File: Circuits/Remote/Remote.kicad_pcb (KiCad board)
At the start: 2 copper layers, 84 x 64 mm, 33 parts, among them CN1 WRITER, Q1 2SK4017, SW1 WakeUp, U1 TWE_LITE_SMD, U2 STEPUPDIP3.3V, U3 ATP3011-PU, U4 HT82V739

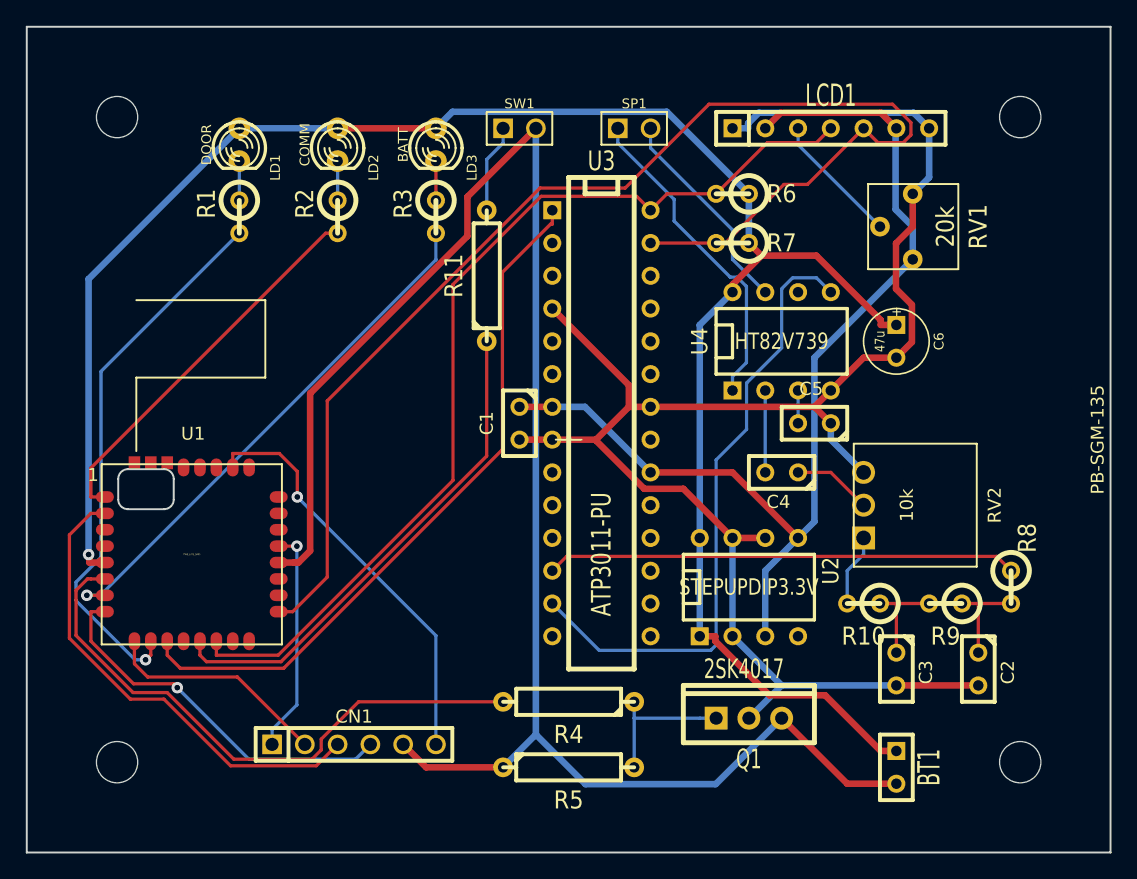
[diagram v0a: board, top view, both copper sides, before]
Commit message: Moved ATP.
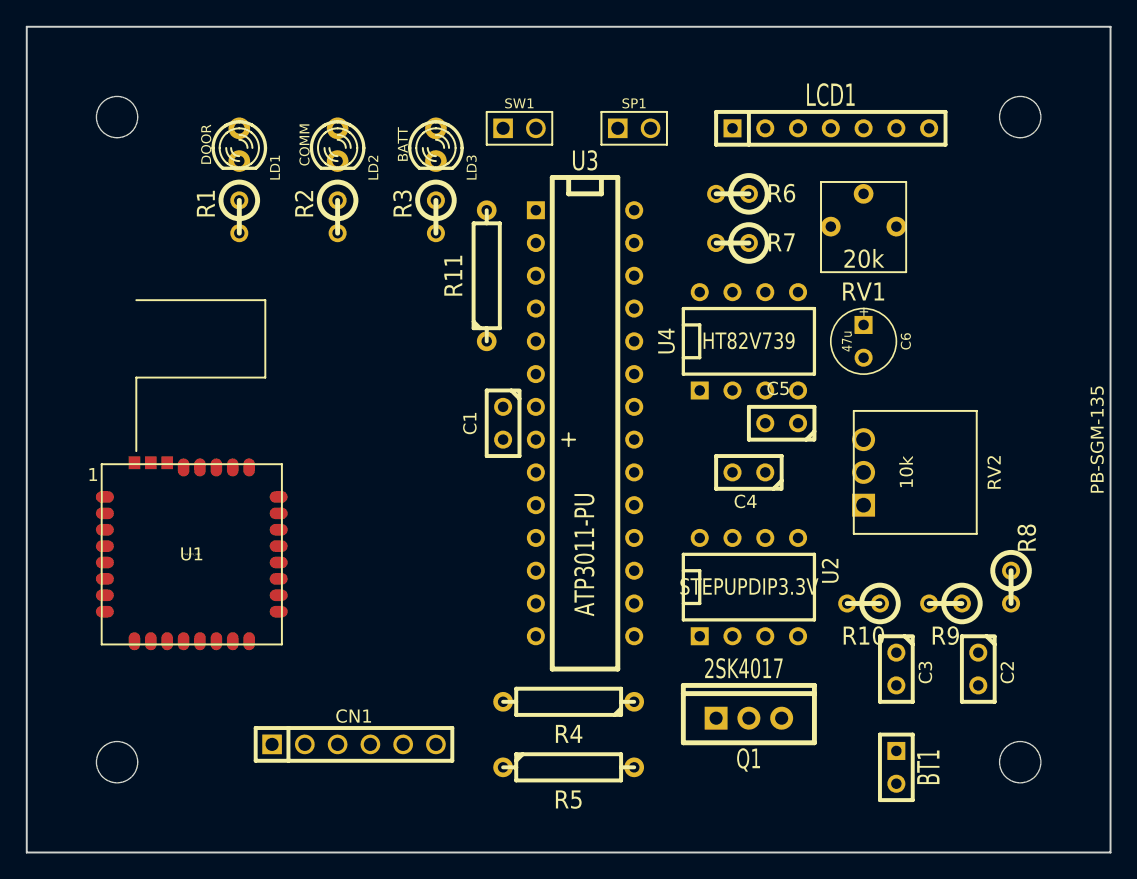
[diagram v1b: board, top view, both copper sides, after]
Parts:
- U1: footprint TWE-001L-SMD -> TWE-001L-SMD-noNTH
- moved RV1 2.84 mm to (80.0, 27.9), turned to 0 degrees
- moved C5 2.54 mm to (73.7, 44.5)
- moved RV2 2.54 mm to (80.0, 48.3)
- moved C4 2.54 mm to (71.1, 48.3)
- moved C6 2.54 mm to (80.0, 38.1)
- moved U4 2.54 mm to (71.1, 38.1)
- moved C1 1.27 mm to (52.1, 44.5)
- moved U3 1.27 mm to (58.4, 44.5)
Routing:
- net VCC: track 151.1 -> 0.00 mm, vias 1 -> 0
- net GND: track 135.6 -> 0.00 mm
- net /QGND: track 133.0 -> 0.00 mm
- net /SDA: track 99.4 -> 0.00 mm
- net /3.3VOUT: track 81.6 -> 0.00 mm
- net /SCL: track 75.4 -> 0.00 mm
- net /RESET#: track 54.7 -> 0.00 mm
- net /PLAY#: track 48.7 -> 0.00 mm
- net /GND_SW: track 45.5 -> 0.00 mm
- net /PWM4: track 42.7 -> 0.00 mm, vias 1 -> 0
- net /PWM1: track 41.3 -> 0.00 mm, vias 1 -> 0
- net /WUP: track 39.0 -> 0.00 mm
- net /PRG: track 37.0 -> 0.00 mm
- net /AOUT: track 36.5 -> 0.00 mm
- net /M2: track 32.3 -> 0.00 mm, vias 1 -> 0
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
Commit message: Re-layout by FreeRouting.
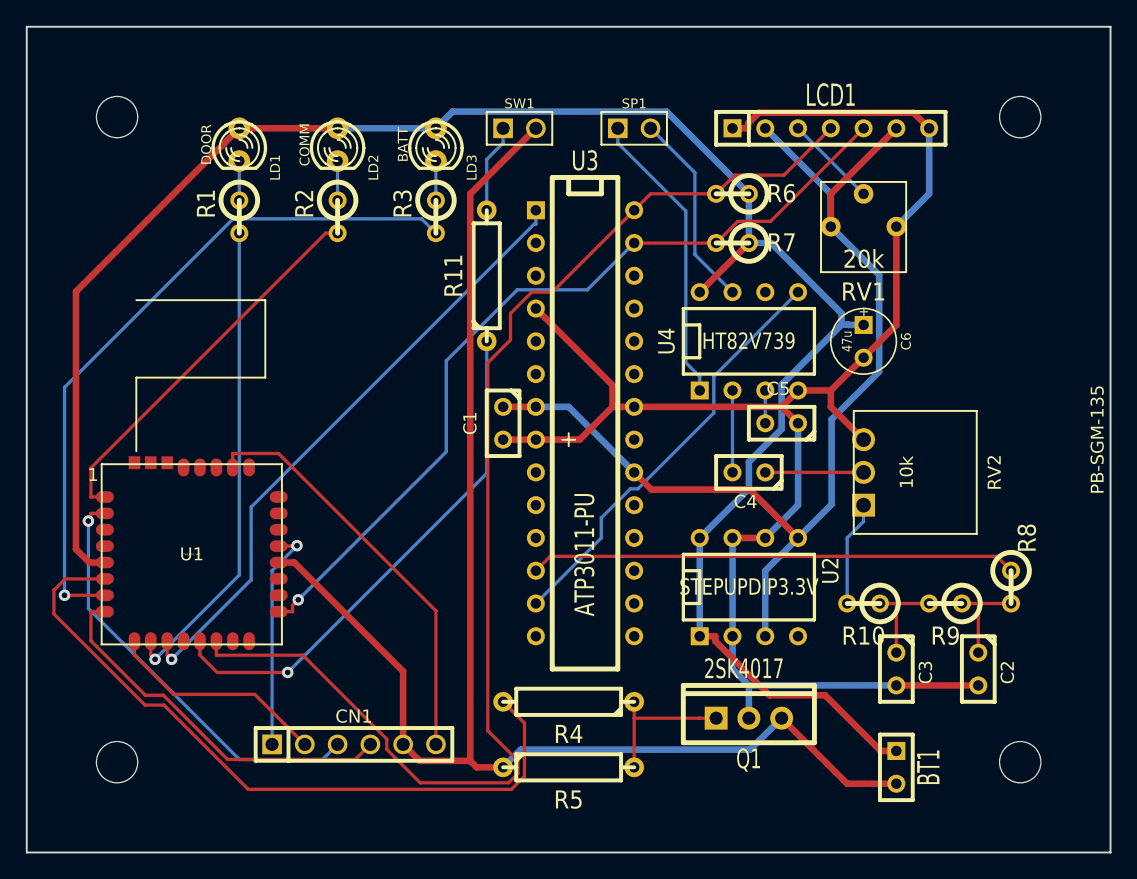
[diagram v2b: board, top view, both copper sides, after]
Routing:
- net VCC: track 0.00 -> 152.3 mm
- net /QGND: track 0.00 -> 128.4 mm
- net GND: track 0.00 -> 112.6 mm
- net /SCL: track 0.00 -> 97.4 mm
- net /3.3VOUT: track 0.00 -> 83.5 mm
- net /SDA: track 0.00 -> 65.3 mm, vias 0 -> 1
- net /GND_SW: track 0.00 -> 55.1 mm
- net /PWM1: track 0.00 -> 53.9 mm, vias 0 -> 1
- net /RESET#: track 0.00 -> 48.1 mm, vias 0 -> 1
- net /WUP: track 0.00 -> 40.5 mm, vias 0 -> 1
- net /AOUT: track 0.00 -> 37.8 mm
- net /PWM4: track 0.00 -> 37.3 mm, vias 0 -> 1
- net /PRG: track 0.00 -> 33.2 mm, vias 0 -> 1
- net /PLAY#: track 0.00 -> 32.9 mm
- net /M2: track 0.00 -> 32.2 mm
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
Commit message: Moved LED out of the PCB via pin header.
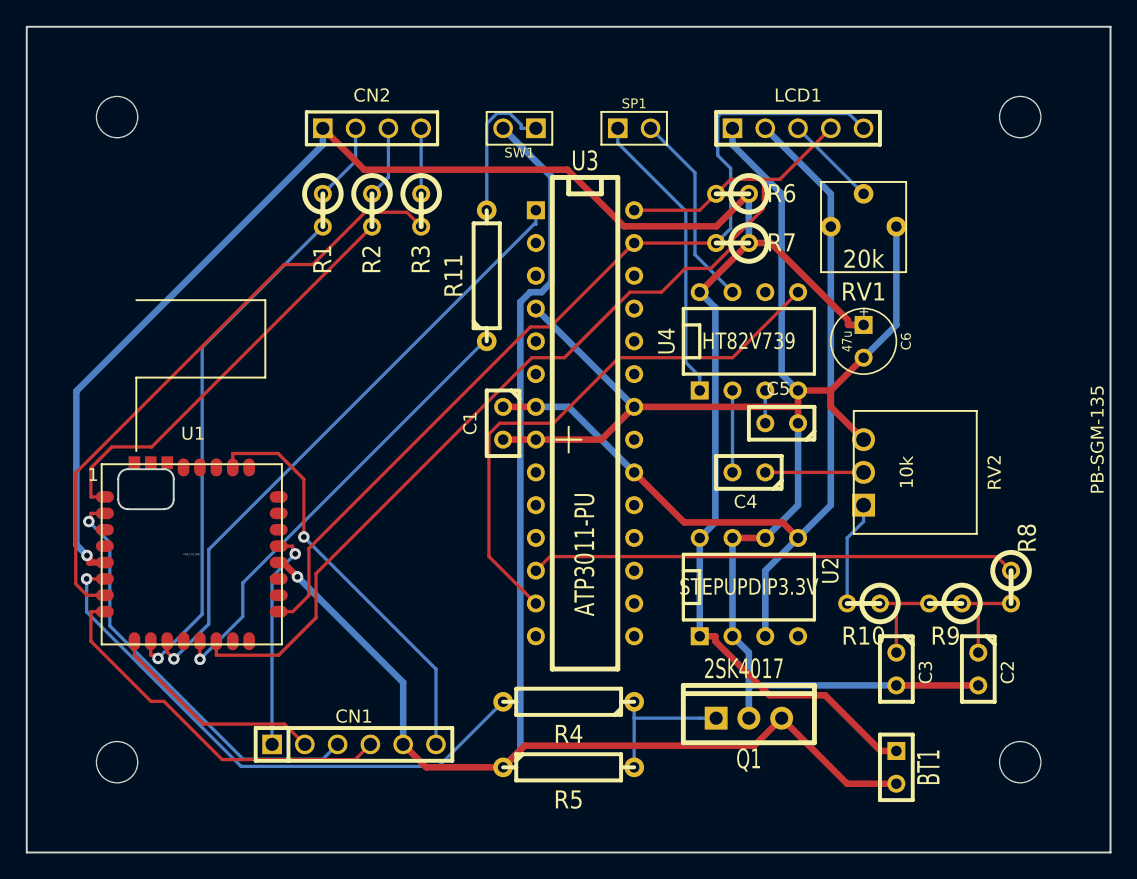
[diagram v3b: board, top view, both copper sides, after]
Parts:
- removed LD1: DOOR, LED-3MM
- removed LD2: COMM, LED-3MM
- removed LD3: BATT, LED-3MM
- added CN2: CONN_4, PIN_ARRAY_4x1, F.Cu at (41.9, 21.6)
- LCD1: footprint SIL-7 -> PIN_ARRAY_5x1
- U1: footprint TWE-001L-SMD-noNTH -> TWE-001L-SMD
- moved R1 6.50 mm to (38.1, 27.9)
- moved R2 2.71 mm to (41.9, 27.9)
- moved LCD1 2.54 mm to (74.9, 21.6)
- moved R3 1.25 mm to (45.7, 27.9)
- turned SW1 to 180 degrees
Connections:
- R1 pad 1: /LD1 -> /DOOR
- R2 pad 1: /LD2 -> /COMM
- R3 pad 1: /LD3 -> /BATT
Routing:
- net /SCL: track 97.4 -> 80.3 mm
- net /3.3VOUT: track 83.5 -> 70.6 mm
- net /GND_SW: track 55.1 -> 43.3 mm, vias 0 -> 1
- net /PLAY#: track 32.9 -> 43.2 mm
- net /PWM1: track 53.9 -> 46.8 mm, vias 1 -> 0
- net /DOOR: track 0.00 -> 6.13 mm
- net /COMM: track 0.00 -> 5.61 mm
- net /SDA: track 65.3 -> 70.4 mm, vias 1 -> 0
- net /WUP: track 40.5 -> 35.4 mm
- net /BATT: track 0.00 -> 5.08 mm
- net /SW: track 6.88 -> 11.5 mm
- net VCC: track 152.3 -> 148.2 mm, vias 0 -> 1
- net /PWM4: track 37.3 -> 40.5 mm
- net /LD3: track 3.05 -> 0.00 mm
- net /LD2: track 3.05 -> 0.00 mm
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
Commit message: Ordered to PCB prototyping service.
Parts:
- DoorChecker Remote: renamed from PB-SGM-135
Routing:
- added copper zone on B.Cu, net (none)
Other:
- board text added: "1"
- board text added: "BT"
- board text added: "CFG"
- board text added: "CM"
- board text added: "Contrast"
- board text added: "DR"
- board text added: "GND"
- board text added: "PRG"
- board text added: "RST"
- board text added: "RXD"
- board text added: "TXD"
- board text added: "Vcc"
- board text added: "Volume"
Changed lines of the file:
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@@
     (links 70)
     (no_connects 0)
-    (area 12.192 12.7 102.108001 78.740001)
+    (area 12.192 12.7 113.092571 86.139)
     (thickness 1)
-    (drawings 0)
+    (drawings 18)
     (tracks 241)
     (zones 0)
@@
     (mod_text_size 1 1)
     (mod_text_width 0.15)
-    (pad_size 1.778 1.778)
-    (pad_drill 1.143)
+    (pad_size 3.2 3.2)
+    (pad_drill 3.2)
     (pad_to_mask_clearance 0)
     (aux_axis_origin 0 0)
     (visible_elements 7FFFFFFF)
     (pcbplotparams
-      (layerselection 3178497)
+      (layerselection 284196865)
       (usegerberextensions true)
       (excludeedgelayer true)
@@
       (plotinvisibletext false)
       (padsonsilk false)
-      (subtractmaskfromsilk false)
+      (subtractmaskfromsilk true)
       (outputformat 1)
       (mirror false)
-      (drillshape 1)
+      (drillshape 0)
       (scaleselection 1)
-      (outputdirectory ""))
+      (outputdirectory gerber/))
   )
   (net 0 "")
@@
       (effects (font (size 0.762 0.762) (thickness 0.1524)))
     )
-    (fp_text value SPEAKER (at 0 -1.905) (layer F.SilkS) hide
+    (fp_text value SPEAKER (at 0.762 2.286) (layer F.SilkS) hide
       (effects (font (size 0.762 0.762) (thickness 0.1524)))
     )
@@
     (descr "Connecteurs 2 pins")
     (tags "CONN DEV")
-    (fp_text reference SW1 (at 0 -1.905 180) (layer F.SilkS)
+    (fp_text reference SW1 (at 0 2.159 180) (layer F.SilkS)
       (effects (font (size 0.762 0.762) (thickness 0.1524)))
     )
@@
     (descr "Double rangee de contacts 2 x 5 pins")
     (tags CONN)
-    (fp_text reference CN2 (at 0 -2.54) (layer F.SilkS)
+    (fp_text reference CN2 (at -8.001 0) (layer F.SilkS)
       (effects (font (size 1.016 1.016) (thickness 0.2032)))
     )
@@
     )
   )
-  (module PB-SGM-135 (layer F.Cu)
-    (at 57.15 45.72)
-    (fp_text reference PB-SGM-135 (at 41 0 90) (layer F.SilkS)
-      (effects (font (size 1 1) (thickness 0.15)))
-    )
-    (fp_text value VAL** (at 0 0) (layer F.SilkS) hide
-      (effects (font (size 1 1) (thickness 0.15)))
-    )
-    (fp_line (start 0 -1) (end 0 1) (layer F.SilkS) (width 0.15))
-    (fp_line (start -1 0) (end 1 0) (layer F.SilkS) (width 0.15))
-    (fp_line (start -42 -32) (end -42 32) (layer Edge.Cuts) (width 0.15))
-    (fp_line (start -42 32) (end 42 32) (layer Edge.Cuts) (width 0.15))
-    (fp_line (start 42 32) (end 42 -32) (layer Edge.Cuts) (width 0.15))
-    (fp_line (start 42 -32) (end -42 -32) (layer Edge.Cuts) (width 0.15))
-    (pad "" np_thru_hole circle (at -35 -25) (size 3.2 3.2) (drill 3.2)
-      (layers *.Cu *.Mask F.SilkS)
-    )
-    (pad "" np_thru_hole circle (at -35 25) (size 3.2 3.2) (drill 3.2)
-      (layers *.Cu *.Mask F.SilkS)
-    )
-    (pad "" np_thru_hole circle (at 35 25) (size 3.2 3.2) (drill 3.2)
-      (layers *.Cu *.Mask F.SilkS)
-    )
-    (pad "" np_thru_hole circle (at 35 -25) (size 3.2 3.2) (drill 3.2)
-      (layers *.Cu *.Mask F.SilkS)
-    )
-    (model SGM-135-Lower.wrl
-      (at (xyz 0 0 0))
-      (scale (xyz 0.393701 0.393701 0.393701))
-      (rotate (xyz 0 0 0))
-    )
-  )
   (module TWE-001L-SMD (layer F.Cu)
     (at 27.94 54.61)
@@
       (effects (font (size 1 1) (thickness 0.15)))
     )
-    (fp_text value TWE_LITE_SMD (at 0 0) (layer F.SilkS)
+    (fp_text value TWE_LITE_SMD (at 0 0.85) (layer F.SilkS)
       (effects (font (size 0.127 0.127) (thickness 0.000001)))
     )
+    (fp_line (start -0.5 0) (end -0.2 0) (layer F.SilkS) (width 0.15))
+    (fp_line (start 0 -0.5) (end 0 -0.2) (layer F.SilkS) (width 0.15))
+    (fp_line (start 0 0.5) (end 0 0.2) (layer F.SilkS) (width 0.15))
+    (fp_line (start 0.2 0) (end 0.5 0) (layer F.SilkS) (width 0.15))
     (fp_text user 1 (at -7.65 -6.15) (layer F.SilkS)
       (effects (font (size 1 1) (thickness 0.15)))
@@
       (rotate (xyz 0 0 0))
     )
+  )
+  (module PB-SGM-135 (layer F.Cu)
+    (at 57.15 45.72)
+    (fp_text reference "DoorChecker Remote" (at 41 0 90) (layer F.SilkS)
+      (effects (font (size 1 1) (thickness 0.15)))
+    )
+    (fp_text value VAL** (at 0 0) (layer F.SilkS) hide
+      (effects (font (size 1 1) (thickness 0.15)))
+    )
+    (fp_line (start 0 -1) (end 0 1) (layer F.SilkS) (width 0.15))
+    (fp_line (start -1 0) (end 1 0) (layer F.SilkS) (width 0.15))
+    (fp_line (start -42 -32) (end -42 32) (layer Edge.Cuts) (width 0.15))
+    (fp_line (start -42 32) (end 42 32) (layer Edge.Cuts) (width 0.15))
+    (fp_line (start 42 32) (end 42 -32) (layer Edge.Cuts) (width 0.15))
+    (fp_line (start 42 -32) (end -42 -32) (layer Edge.Cuts) (width 0.15))
+    (pad "" np_thru_hole circle (at -35 -25) (size 3.2 3.2) (drill 3.2)
+      (layers *.Cu *.Mask F.SilkS)
+      (clearance 1.4)
+    )
+    (pad "" np_thru_hole circle (at -35 25) (size 3.2 3.2) (drill 3.2)
+      (layers *.Cu *.Mask F.SilkS)
+      (clearance 1.4)
+    )
+    (pad "" np_thru_hole circle (at 35 25) (size 3.2 3.2) (drill 3.2)
+      (layers *.Cu *.Mask F.SilkS)
+      (clearance 1.4)
+    )
+    (pad "" np_thru_hole circle (at 35 -25) (size 3.2 3.2) (drill 3.2)
+      (layers *.Cu *.Mask F.SilkS)
+      (clearance 1.4)
+    )
+  )
+  (gr_text CFG (at 46.99 73.914 90) (layer F.SilkS)
+    (effects (font (size 1.5 1.5) (thickness 0.3)))
+  )
+  (gr_text GND (at 44.45 73.914 90) (layer F.SilkS)
+    (effects (font (size 1.5 1.5) (thickness 0.3)))
+  )
+  (gr_text TXD (at 42.164 73.66 90) (layer F.SilkS)
+    (effects (font (size 1.5 1.5) (thickness 0.3)))
+  )
+  (gr_text PRG (at 39.624 73.914 90) (layer F.SilkS)
+    (effects (font (size 1.5 1.5) (thickness 0.3)))
+  )
+  (gr_text RXD (at 37.084 73.914 90) (layer F.SilkS)
+    (effects (font (size 1.5 1.5) (thickness 0.3)))
+  )
+  (gr_text RST (at 34.29 73.914 90) (layer F.SilkS)
+    (effects (font (size 1.5 1.5) (thickness 0.3)))
+  )
+  (gr_text Volume (at 87.122 41.91) (layer F.SilkS)
+    (effects (font (size 1 1) (thickness 0.2)))
+  )
+  (gr_text Contrast (at 87.376 31.496) (layer F.SilkS)
+    (effects (font (size 1 1) (thickness 0.2)))
+  )
+  (gr_text 1 (at 54.356 25.908) (layer F.SilkS)
+    (effects (font (size 1 1) (thickness 0.2)))
+  )
+  (gr_text 1 (at 65.278 41.91 90) (layer F.SilkS)
+    (effects (font (size 1 1) (thickness 0.2)))
+  )
+  (gr_text 1 (at 65.532 60.96 90) (layer F.SilkS)
+    (effects (font (size 1 1) (thickness 0.2)))
+  )
+  (gr_text 1 (at 69.85 19.05) (layer F.SilkS)
+    (effects (font (size 1.5 1.5) (thickness 0.3)))
+  )
+  (gr_text BT (at 45.72 18.288 90) (layer F.SilkS)
+    (effects (font (size 1.5 1.5) (thickness 0.3)))
+  )
+  (gr_text CM (at 43.18 18.288 90) (layer F.SilkS)
+    (effects (font (size 1.5 1.5) (thickness 0.3)))
+  )
+  (gr_text DR (at 40.64 18.288 90) (layer F.SilkS)
+    (effects (font (size 1.5 1.5) (thickness 0.3)))
+  )
+  (gr_text Vcc (at 38.1 17.78 90) (layer F.SilkS)
+    (effects (font (size 1.5 1.5) (thickness 0.3)))
+  )
+  (dimension 64.008 (width 0.3) (layer Eco2.User)
+    (gr_text 64.008mm (at 107.013999 45.72 270) (layer Eco2.User)
+      (effects (font (size 1.5 1.5) (thickness 0.3)))
+    )
+    (feature1 (pts (xy 99.187 77.724) (xy 108.363999 77.724)))
+    (feature2 (pts (xy 99.187 13.716) (xy 108.363999 13.716)))
+    (crossbar (pts (xy 105.663999 13.716) (xy 105.663999 77.724)))
+    (arrow1a (pts (xy 105.663999 77.724) (xy 105.077579 76.597497)))
+    (arrow1b (pts (xy 105.663999 77.724) (xy 106.250419 76.597497)))
+    (arrow2a (pts (xy 105.663999 13.716) (xy 105.077579 14.842503)))
+    (arrow2b (pts (xy 105.663999 13.716) (xy 106.250419 14.842503)))
+  )
+  (dimension 84.074 (width 0.3) (layer Eco2.User)
+    (gr_text 84.074mm (at 57.15 84.788999) (layer Eco2.User)
+      (effects (font (size 1.5 1.5) (thickness 0.3)))
+    )
+    (feature1 (pts (xy 99.187 77.724) (xy 99.187 86.138999)))
+    (feature2 (pts (xy 15.113 77.724) (xy 15.113 86.138999)))
+    (crossbar (pts (xy 15.113 83.438999) (xy 99.187 83.438999)))
+    (arrow1a (pts (xy 99.187 83.438999) (xy 98.060497 84.025419)))
+    (arrow1b (pts (xy 99.187 83.438999) (xy 98.060497 82.852579)))
+    (arrow2a (pts (xy 15.113 83.438999) (xy 16.239503 84.025419)))
+    (arrow2b (pts (xy 15.113 83.438999) (xy 16.239503 82.852579)))
   )
   (segment (start 77.47 26.67) (end 77.47 29.21) (width 0.508) (layer B.Cu) (net 1))
@@
     (polygon
       (pts
-        (xy 25.4 78.74) (xy 12.192 78.74) (xy 12.192 67.056) (xy 25.4 67.056)
+        (xy 25.146 78.74) (xy 12.192 78.74) (xy 12.192 67.691) (xy 25.146 67.691)
       )
     )
@@
     (connect_pads (clearance 0.508))
     (min_thickness 0.254)
-    (keepout (tracks not_allowed) (vias not_allowed) (copperpour allowed))
+    (keepout (tracks not_allowed) (vias not_allowed) (copperpour not_allowed))
     (fill (arc_segments 16) (thermal_gap 0.508) (thermal_bridge_width 0.508))
     (polygon
       (pts
-        (xy 21.971 47.625) (xy 26.67 47.625) (xy 26.67 48.768) (xy 26.67 51.435) (xy 21.971 51.435)
+        (xy 22.098 47.879) (xy 26.67 47.879) (xy 26.67 48.768) (xy 26.67 51.308) (xy 22.098 51.308)
       )
     )
@@
     (polygon
       (pts
-        (xy 25.4 67.056) (xy 12.192 67.056) (xy 12.192 78.74) (xy 25.4 78.74)
+        (xy 25.146 67.691) (xy 12.192 67.691) (xy 12.192 78.74) (xy 25.146 78.74)
       )
     )
@@
       )
     )
+  )
+  (zone (net 0) (net_name "") (layer B.Cu) (hatch edge 0.508)
+    (connect_pads yes (clearance 0.508))
+    (min_thickness 0.254)
+    (fill (arc_segments 16) (thermal_gap 0.508) (thermal_bridge_width 0.508))
+    (polygon
+      (pts
+        (xy 42.799 68.199) (xy 15.367 68.199) (xy 15.367 39.624) (xy 42.926 39.624)
+      )
+    )
